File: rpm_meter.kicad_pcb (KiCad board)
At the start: 2 copper layers, 153.8 x 95.2 mm, 126 parts, among them IC1 SN74LV1T34DCKR, IC2 ISO6521FREUR, IC6 TPS566247DRLR, J1 Conn_01x01_Socket, J2 Conn_2Rows-05Pins, J3 Conn_01x01_Socket, J4 Conn_01x01_Socket, J5 Conn_01x01_Socket, J6 Conn_01x01_Socket, J7 Conn_01x01_Socket, Q1 BC846, Q14 BC846, Q15 BC846, Q16 BC846, SW1 RotaryEncoder_Switch_MP, U1 M24C02-RMN, U2 STM32C031C6Tx, U3 74LVC1G123, U4 TLV1117-33, U5 FT231XQ, Y1 8

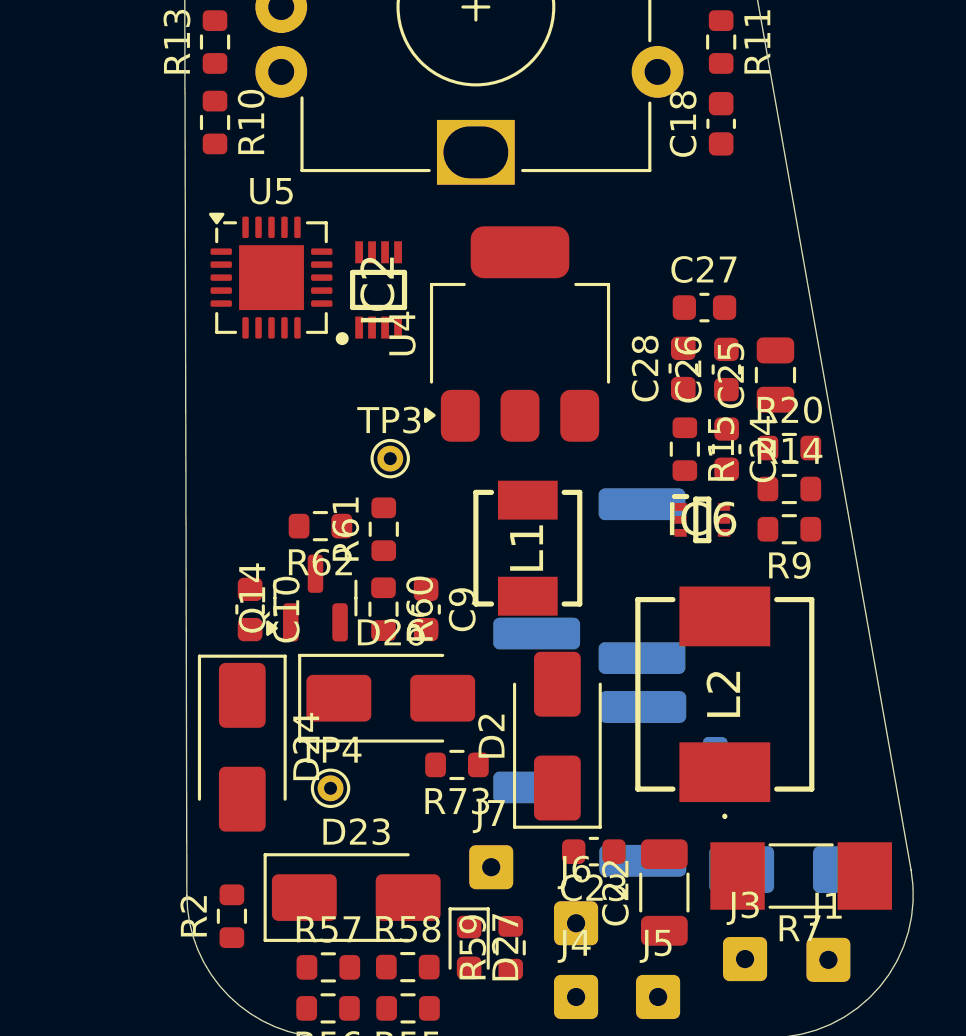
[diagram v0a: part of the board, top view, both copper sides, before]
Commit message: USB C connector
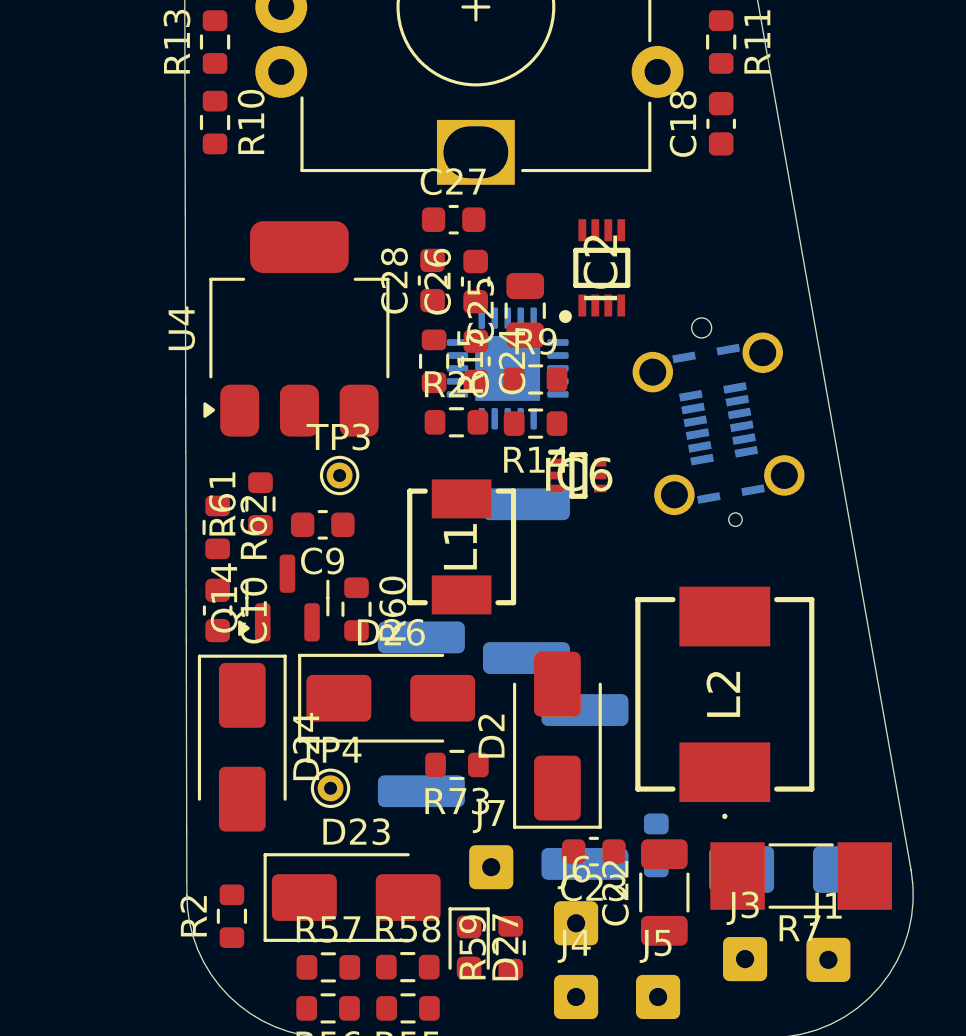
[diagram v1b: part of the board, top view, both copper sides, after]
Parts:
- added J8: UJ20-C-V-C-1-SMT-TR, Library_local:UJ20CVC1SMTTR, B.Cu at (214.4, 101.2)
- U5: moved to B.Cu
- moved LOGO1 16.1 mm to (204.3, 90.8)
- moved R20 12.9 mm to (204.3, 101.2)
- moved R9 11.4 mm to (207.4, 99.5), turned to 0 degrees
- moved C24 10.2 mm to (205.1, 98.8)
- moved C27 10.2 mm to (204.2, 93.3)
- moved C28 10.2 mm to (203.4, 95.7)
- moved R15 10.2 mm to (203.5, 98.8)
- moved C26 10.2 mm to (205.1, 95.7)
- moved R14 10.1 mm to (207.4, 101.2), turned to 180 degrees
- moved C25 9.95 mm to (207.0, 96.8)
- moved U5 9.75 mm to (206.3, 99.1), turned to 180 degrees
- moved IC2 8.64 mm to (209.9, 95.2)
- moved U4 8.50 mm to (198.3, 97.5)
- moved C9 5.14 mm to (199.2, 105.1), turned to 180 degrees
- moved IC6 5.07 mm to (209.1, 103.2)
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
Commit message: stm32c031g6u6
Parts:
- removed U2: STM32C031C6Tx, Package_QFP:LQFP-48_7x7mm_P0.5mm
- added U6: STM32C031G6Ux, Package_DFN_QFN:QFN-28_4x4mm_P0.5mm, F.Cu at (204.1, 52.4)
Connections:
- C6 pad 1: /mcu/NRST -> GND
- C6 pad 2: GND -> /mcu/NRST

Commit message: New version
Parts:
- U6: footprint Package_DFN_QFN:QFN-28_4x4mm_P0.5mm -> Library_local:QFN-28_4x4mm_P0.5mm
- moved TP5 10.3 mm to (200.1, 56.4)
- moved IC1 7.46 mm to (200.8, 49.7)
- moved C12 3.95 mm to (207.0, 59.1)
- moved R64 3.95 mm to (206.2, 61.5)
- moved R65 3.95 mm to (205.4, 59.1)
- moved R70 3.95 mm to (203.8, 60.7)
- moved C14 3.95 mm to (202.2, 60.7)
- moved R71 3.95 mm to (202.9, 58.4)
- moved C17 2.64 mm to (209.6, 67.5)
- moved U3 2.59 mm to (209.7, 63.9)
- moved R63 1.98 mm to (206.1, 65.0)
- moved C11 1.90 mm to (206.1, 66.7)
- moved R76 1.88 mm to (203.0, 65.1)
- moved R75 1.88 mm to (202.9, 68.3)
- moved C16 1.88 mm to (202.9, 66.7)
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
